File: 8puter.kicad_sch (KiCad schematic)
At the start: 11 parts, among them J1 PWR-DC

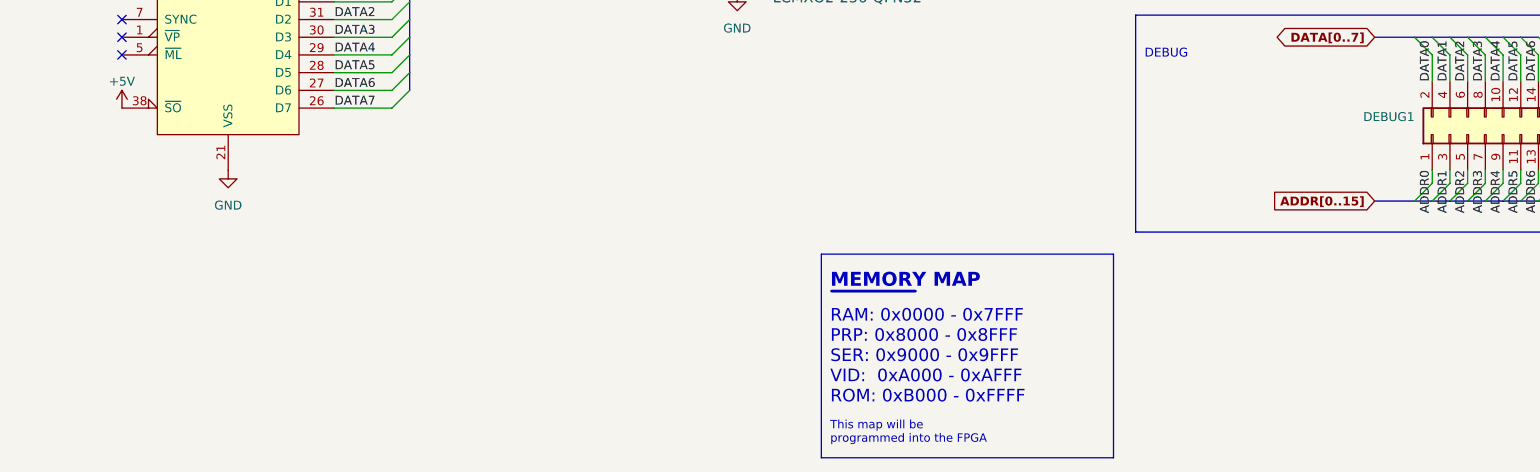
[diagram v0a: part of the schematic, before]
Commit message: Pulldowns, minor reroute
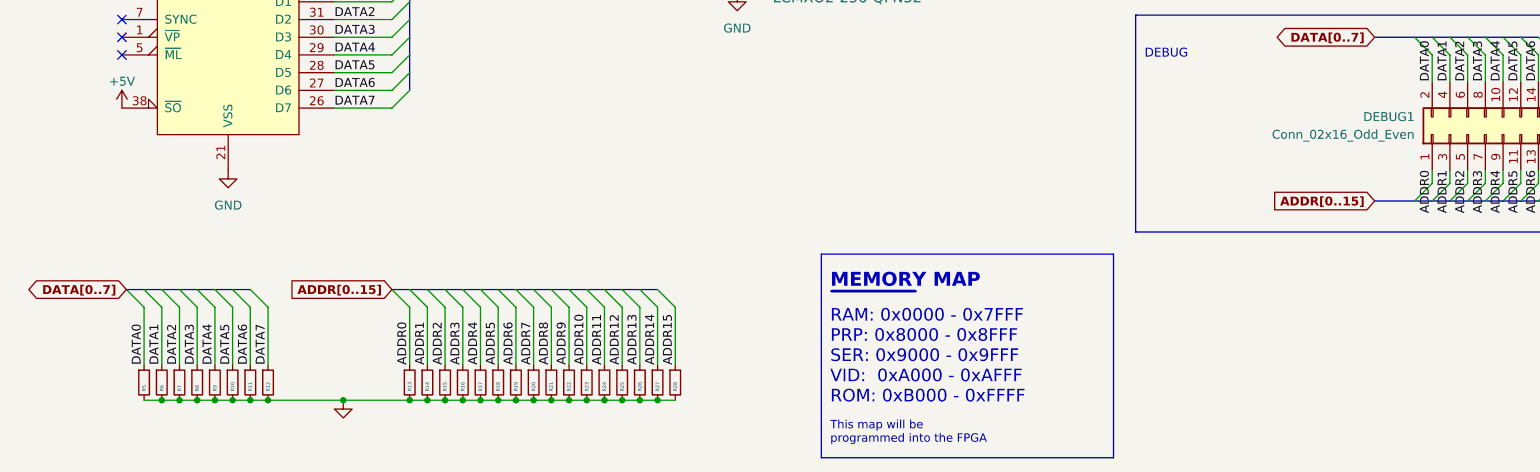
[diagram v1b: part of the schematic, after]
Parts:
- added R10, R11, R12, R13, R14, R15, R16, R17, R18, R19, R20, R21, R22, R23, R24, R25, R26, R27, R28, R5, R6, R7, R8, R9: (no value), symbol Device:R_Small
- DEBUG1: value (none) -> Conn_02x16_Odd_Even; footprint (none) -> Connector_PinHeader_2.00mm:PinHeader_2x16_P2.00mm_Vertical
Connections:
- net ADDR0: now also R13.1
- net ADDR1: now also R14.1
- net ADDR10: now also R23.1
- net ADDR11: now also R24.1
- net ADDR12: now also R25.1
- net ADDR13: now also R26.1
- net ADDR14: now also R27.1
- net ADDR15: now also R28.1
- net ADDR2: now also R15.1
- net ADDR3: now also R16.1
- net ADDR4: now also R17.1
- net ADDR5: now also R18.1
- net ADDR6: now also R19.1
- net ADDR7: now also R20.1
- net ADDR8: now also R21.1
- net ADDR9: now also R22.1
- net DATA0: now also R5.1
- net DATA1: now also R6.1
- net DATA2: now also R7.1
- net DATA3: now also R8.1
- net DATA4: now also R9.1
- net DATA5: now also R10.1
- net DATA6: now also R11.1
- net DATA7: now also R12.1
- net GND: now also R10.2, R11.2, R12.2, R13.2, R14.2, R15.2, R16.2, R17.2, R18.2, R19.2, R20.2, R21.2, R22.2, R23.2, R24.2, R25.2, R26.2, R27.2, R28.2, R5.2, R6.2, R7.2, R8.2, R9.2

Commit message: Update readme
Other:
- note added: "Incomplete"
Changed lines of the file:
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@@
     (effects (font (size 1.27 1.27)) (justify left bottom))
+  )
+  (text "Incomplete" (at 203.2 46.355 0)
+    (effects (font (size 1.27 1.27) (thickness 0.254) bold) (justify left bottom))
   )
   (text "RAM: 0x0000 - 0x7FFF\nPRP: 0x8000 - 0x8FFF\nSER: 0x9000 - 0x9FFF\nVID:  0xA000 - 0xAFFF\nROM: 0xB000 - 0xFFFF"
@@
     (effects (font (size 2 2) (thickness 0.4) bold) (justify left bottom))
   )
+  (text "Incomplete" (at 40.005 34.29 0)
+    (effects (font (size 1.27 1.27) (thickness 0.254) bold) (justify left bottom))
+  )
   (text "This map will be \nprogrammed into the FPGA" (at 133.35 193.675 0)
     (effects (font (size 1.2 1.2)) (justify left bottom))
+  )
+  (text "Incomplete" (at 106.045 33.655 0)
+    (effects (font (size 1.27 1.27) (thickness 0.254) bold) (justify left bottom))
   )
   (text "CPU" (at 48.895 73.025 0)
     (effects (font (size 3 3) (thickness 0.6) bold) (justify left bottom))
   )
+  (text "Incomplete" (at 254 106.045 0)
+    (effects (font (size 1.27 1.27) (thickness 0.254) bold) (justify left bottom))
+  )
   (label "DATA5" (at 232.41 141.605 90)

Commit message: First completed routing
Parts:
- removed CRYSTAL0: ACO-10MHz-A, Oscillator:Oscillator_DIP-14_LargePads, symbol Oscillator:ACO-xxxMHz-A
- added X1: (no value), symbol Oscillator:CXO_DIP8
- C3: value 10uF 16V -> (none); footprint Capacitor_THT:CP_Radial_D8.0mm_P5.00mm -> (none)
- R10, R11, R12, R13, R14, R15, R16, R17, R18, R19, R20, R21, R22, R23, R24, R25, R26, R27, R28, R5, R6, R7, R8, R9: value (none) -> 10K; footprint (none) -> Resistor_SMD:R_0805_2012Metric
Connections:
- net +5V: now also X1.1 (EN), X1.8 (Vcc)
- net Clock/CRYSTAL: now also X1.5 (OUT)
- net GND: now also X1.4 (GND)
- no-connect marks 9 -> 8
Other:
- sheet Clock ports: added none; removed ~{CLOCK}
- sheet Power ports: added 3V; removed none
- sheet Video ports: added CLOCK, ~{RESET}; removed none

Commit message: Gerber Plots
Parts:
- C3: value (none) -> 10uF 16V; footprint (none) -> Capacitor_THT:CP_Radial_D5.0mm_P2.50mm
- JTAG1: value PIN_HDR -> (none); footprint Connector_PinHeader_1.00mm:PinHeader_1x05_P1.00mm_Vertical -> (none)
- X1: value (none) -> ECS-2200BX-100; footprint (none) -> Oscillator:Oscillator_DIP-8
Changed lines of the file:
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@@
       (effects (font (size 1.27 1.27)) (justify left))
     )
-    (property "Value" "" (id 1) (at 20.32 42.545 0)
-      (effects (font (size 1.27 1.27)) (justify left))
-    )
-    (property "Footprint" "" (id 2) (at 31.75 42.545 0)
+    (property "Value" "10uF 16V" (id 1) (at 20.32 42.545 0)
+      (effects (font (size 1.27 1.27)) (justify left))
+    )
+    (property "Footprint" "Capacitor_THT:CP_Radial_D5.0mm_P2.50mm" (id 2) (at 31.75 42.545 0)
       (effects (font (size 1.27 1.27)) hide)
     )
@@
       (effects (font (size 1.27 1.27)) (justify right))
     )
-    (property "Value" "" (id 1) (at 97.79 29.845 0)
+    (property "Value" "ECS-2200BX-100" (id 1) (at 97.79 29.845 0)
       (effects (font (size 1.27 1.27)) (justify right))
     )
-    (property "Footprint" "" (id 2) (at 112.395 45.72 0)
+    (property "Footprint" "Oscillator:Oscillator_DIP-8" (id 2) (at 112.395 45.72 0)
       (effects (font (size 1.27 1.27)) hide)
     )
@@
       (effects (font (size 1.27 1.27)) (justify left))
     )
-    (property "Value" "PIN_HDR" (id 1) (at 161.925 86.36 0)
-      (effects (font (size 1.27 1.27)) (justify left))
-    )
-    (property "Footprint" "Connector_PinHeader_1.00mm:PinHeader_1x05_P1.00mm_Vertical" (id 2) (at 153.035 94.615 0)
+    (property "Value" "" (id 1) (at 161.925 86.36 0)
+      (effects (font (size 1.27 1.27)) (justify left))
+    )
+    (property "Footprint" "" (id 2) (at 153.035 94.615 0)
       (effects (font (size 1.27 1.27)) hide)
     )
@@
       (effects (font (size 1.27 1.27)) hide)
     )
-    (property "Value" "" (id 1) (at 57.15 31.115 90)
+    (property "Value" "+3V0" (id 1) (at 57.15 31.115 90)
       (effects (font (size 1.27 1.27)) (justify left))
     )
@@
     )
     (path "/93319bf6-31a0-4369-8170-29673b7ed1a4"
-      (reference "JTAG1") (unit 1) (value "PIN_HDR") (footprint "Connector_PinHeader_1.00mm:PinHeader_1x05_P1.00mm_Vertical")
+      (reference "JTAG1") (unit 1) (value "PIN_HDR") (footprint "Connector_PinHeader_2.00mm:PinHeader_1x05_P2.00mm_Vertical")
     )
     (path "/287b8d7b-7977-45e3-a8a2-fb0a63aeaa82/29f5a9a2-94a6-4cdc-a8e7-84648a7a8222"

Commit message: board improvements
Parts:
- JTAG1: value (none) -> PIN_HDR; footprint (none) -> Connector_PinHeader_2.00mm:PinHeader_1x05_P2.00mm_Vertical
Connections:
- net CLOCK: no longer DEBUG1.32 (Pin_32)
- net RDY: now also DEBUG1.32 (Pin_32); no longer DEBUG1.30 (Pin_30)
- net ~{IRQ}: now also DEBUG1.30 (Pin_30)
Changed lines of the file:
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@@
     )
   )
-  (global_label "RDY" (shape bidirectional) (at 255.27 141.605 90) (fields_autoplaced)
+  (global_label "RDY" (shape bidirectional) (at 257.81 141.605 90) (fields_autoplaced)
     (effects (font (size 1.27 1.27)) (justify left))
-    (property "Intersheet References" "${INTERSHEET_REFS}" (id 0) (at 255.3494 135.5633 90)
+    (property "Intersheet References" "${INTERSHEET_REFS}" (id 0) (at 257.8894 135.5633 90)
       (effects (font (size 1.27 1.27)) (justify left) hide)
     )
@@
     )
   )
-  (global_label "CLOCK" (shape input) (at 257.81 141.605 90) (fields_autoplaced)
-    (effects (font (size 1.27 1.27)) (justify left))
-    (property "Intersheet References" "${INTERSHEET_REFS}" (id 0) (at 257.7306 133.0233 90)
-      (effects (font (size 1.27 1.27)) (justify left) hide)
-    )
-  )
   (global_label "~{RESET}" (shape input) (at 31.75 84.455 180) (fields_autoplaced)
     (effects (font (size 1.27 1.27)) (justify right))
@@
     (effects (font (size 1.27 1.27)) (justify left))
     (property "Intersheet References" "${INTERSHEET_REFS}" (id 0) (at 155.3876 114.8556 0)
+      (effects (font (size 1.27 1.27)) (justify left) hide)
+    )
+  )
+  (global_label "~{IRQ}" (shape input) (at 255.27 141.605 90) (fields_autoplaced)
+    (effects (font (size 1.27 1.27)) (justify left))
+    (property "Intersheet References" "${INTERSHEET_REFS}" (id 0) (at 255.1906 135.9867 90)
       (effects (font (size 1.27 1.27)) (justify left) hide)
     )
@@
       (effects (font (size 1.27 1.27)) (justify left))
     )
-    (property "Value" "" (id 1) (at 161.925 86.36 0)
-      (effects (font (size 1.27 1.27)) (justify left))
-    )
-    (property "Footprint" "" (id 2) (at 153.035 94.615 0)
+    (property "Value" "PIN_HDR" (id 1) (at 161.925 86.36 0)
+      (effects (font (size 1.27 1.27)) (justify left))
+    )
+    (property "Footprint" "Connector_PinHeader_2.00mm:PinHeader_1x05_P2.00mm_Vertical" (id 2) (at 153.035 94.615 0)
       (effects (font (size 1.27 1.27)) hide)
     )
@@
       (reference "#PWR014") (unit 1) (value "GND") (footprint "")
     )
-    (path "/59d6507d-8c01-4b37-beee-b798f6eef3f6/55dd627f-148e-4776-a40a-a7f9e57cdaf5"
-      (reference "#PWR021") (unit 1) (value "GND") (footprint "")
-    )
     (path "/6fb476cc-0d35-4ef8-90a2-1a1fd6ffea47/e2a78a6e-e8db-42b7-9254-326091c204ad"

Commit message: some docs
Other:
- removed sheet Serial Controller
- sheet Peripheral Handler ports: added CLOCK, ~{SERIAL_CS}, ~{SRL_IRQ}; removed CLK
- note added: "10K Pulldowns for DATA and ADDR buses"
- note removed: "Incomplete"

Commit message: serial rollback
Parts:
- removed GLUE_FPGA1: LCMXO2-256-QFN32, Package_DFN_QFN:QFN-32-1EP_5x5mm_P0.5mm_EP3.1x3.1mm, symbol Custom:﻿MachXO2-256-QFN32
- removed JTAG1: PIN_HDR, Connector_PinHeader_2.00mm:PinHeader_1x05_P2.00mm_Vertical, symbol Connector_Generic:Conn_01x05
- removed R1: 1K, Resistor_SMD:R_0805_2012Metric, symbol Device:R
- removed R3: 4.7K, Resistor_SMD:R_0805_2012Metric, symbol Device:R
- added U1: 74HC00, symbol 74xx:74HC00
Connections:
- net +5V: now also U1.14 (VCC)
- net ADDR14: now also U1.10
- net ADDR15: now also U1.4, U1.5
- net CLOCK: now also U1.1
- net GND: now also C3.1, U1.7 (GND); no longer C3.2
- net Power/PWR: now also C3.2; no longer C3.1
- net ~{PRP_CS}: now also U1.8
- net ~{RAM_CS}: now also U1.3
- net ~{ROM_CS}: now also U1.2, U1.6, U1.9
- no-connect marks 8 -> 5
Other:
- added sheet Storage (sch/storage.kicad_sch)
- sheet Memory Unit ports: added BUS_R~{W}; removed ~{BUS_READ}, ~{BUS_WRITE}
- sheet Peripheral Handler ports: added none; removed ~{SERIAL_CS}, ~{SRL_IRQ}
- sheet Power ports: added none; removed 3V
- sheet Video ports: added A[0..15]; removed none
- note added: "RAM: 0x0000 - 0x3FFF VIA: 0x6000 - 0x600F SER: 0x5000 - 0x500F VID: 0x4800 - 0x480F ROM: 0x8000 - 0xFFFF"
- note removed: "RAM: 0x0000 - 0x7FFF PRP: 0x8000 - 0x8FFF SER: 0x9000 - 0x9FFF VID: 0xA000 - 0xAFFF ROM: 0xB000 - 0xFFFF"
- note removed: "This map will be programmed into the FPGA"
- moved on the sheet: C3, R10, R11, R12, R13, R14, R15, R16, R17, R18, R19, R20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
